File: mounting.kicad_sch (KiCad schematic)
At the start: 4 parts

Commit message: Initial component placement
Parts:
- H1, H2, H3, H4: footprint (none) -> MountingHole:MountingHole_2.2mm_M2_DIN965
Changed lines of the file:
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@@
 			)
 		)
-		(property "Footprint" ""
+		(property "Footprint" "MountingHole:MountingHole_2.2mm_M2_DIN965"
 			(at 128.27 88.9 0)
 			(effects
@@
 			)
 		)
-		(property "Footprint" ""
+		(property "Footprint" "MountingHole:MountingHole_2.2mm_M2_DIN965"
 			(at 93.98 78.74 0)
 			(effects
@@
 			)
 		)
-		(property "Footprint" ""
+		(property "Footprint" "MountingHole:MountingHole_2.2mm_M2_DIN965"
 			(at 128.27 78.74 0)
 			(effects
@@
 			)
 		)
-		(property "Footprint" ""
+		(property "Footprint" "MountingHole:MountingHole_2.2mm_M2_DIN965"
 			(at 93.98 88.9 0)
 			(effects

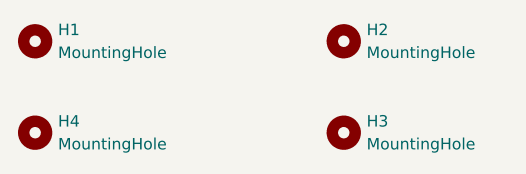
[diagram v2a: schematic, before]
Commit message: Resolve ERC warnings
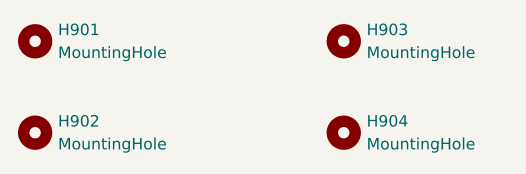
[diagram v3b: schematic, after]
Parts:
- renumbered H1 to H901, H4 to H902, H2 to H903, H3 to H904
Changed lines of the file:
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@@
 		(dnp no)
 		(fields_autoplaced yes)
-		(property "Reference" "H3"
+		(property "Reference" "H904"
 			(at 130.81 87.6299 0)
 			(effects
@@
 			(project ""
 				(path "/16b3e55a-9d75-49bf-a6fe-25414eb3d7da/a359fce7-335c-4dc7-9a29-9985e30edce2"
-					(reference "H3")
+					(reference "H904")
 					(unit 1)
 				)
@@
 		(dnp no)
 		(fields_autoplaced yes)
-		(property "Reference" "H1"
+		(property "Reference" "H901"
 			(at 96.52 77.4699 0)
 			(effects
@@
 			(project ""
 				(path "/16b3e55a-9d75-49bf-a6fe-25414eb3d7da/a359fce7-335c-4dc7-9a29-9985e30edce2"
-					(reference "H1")
+					(reference "H901")
 					(unit 1)
 				)
@@
 		(dnp no)
 		(fields_autoplaced yes)
-		(property "Reference" "H2"
+		(property "Reference" "H903"
 			(at 130.81 77.4699 0)
 			(effects
@@
 			(project ""
 				(path "/16b3e55a-9d75-49bf-a6fe-25414eb3d7da/a359fce7-335c-4dc7-9a29-9985e30edce2"
-					(reference "H2")
+					(reference "H903")
 					(unit 1)
 				)
@@
 		(dnp no)
 		(fields_autoplaced yes)
-		(property "Reference" "H4"
+		(property "Reference" "H902"
 			(at 96.52 87.6299 0)
 			(effects
@@
 			(project ""
 				(path "/16b3e55a-9d75-49bf-a6fe-25414eb3d7da/a359fce7-335c-4dc7-9a29-9985e30edce2"
-					(reference "H4")
-					(unit 1)
-				)
+					(reference "H902")
+					(unit 1)
+				)

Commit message: Footprint selection
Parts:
- H901, H902, H903, H904: footprint MountingHole:MountingHole_2.2mm_M2_DIN965 -> MountingHole:MountingHole_2mm
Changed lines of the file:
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@@
 			)
 		)
-		(property "Footprint" "MountingHole:MountingHole_2.2mm_M2_DIN965"
+		(property "Footprint" "MountingHole:MountingHole_2mm"
 			(at 128.27 88.9 0)
 			(effects
@@
 			)
 		)
-		(property "Footprint" "MountingHole:MountingHole_2.2mm_M2_DIN965"
+		(property "Footprint" "MountingHole:MountingHole_2mm"
 			(at 93.98 78.74 0)
 			(effects
@@
 			)
 		)
-		(property "Footprint" "MountingHole:MountingHole_2.2mm_M2_DIN965"
+		(property "Footprint" "MountingHole:MountingHole_2mm"
 			(at 128.27 78.74 0)
 			(effects
@@
 			)
 		)
-		(property "Footprint" "MountingHole:MountingHole_2.2mm_M2_DIN965"
+		(property "Footprint" "MountingHole:MountingHole_2mm"
 			(at 93.98 88.9 0)
 			(effects
